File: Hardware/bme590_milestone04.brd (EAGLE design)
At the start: 100 x 80 mm, 9 parts, among them IC1 LM317LZ, U1 ARDUINOR3-DIMENSION

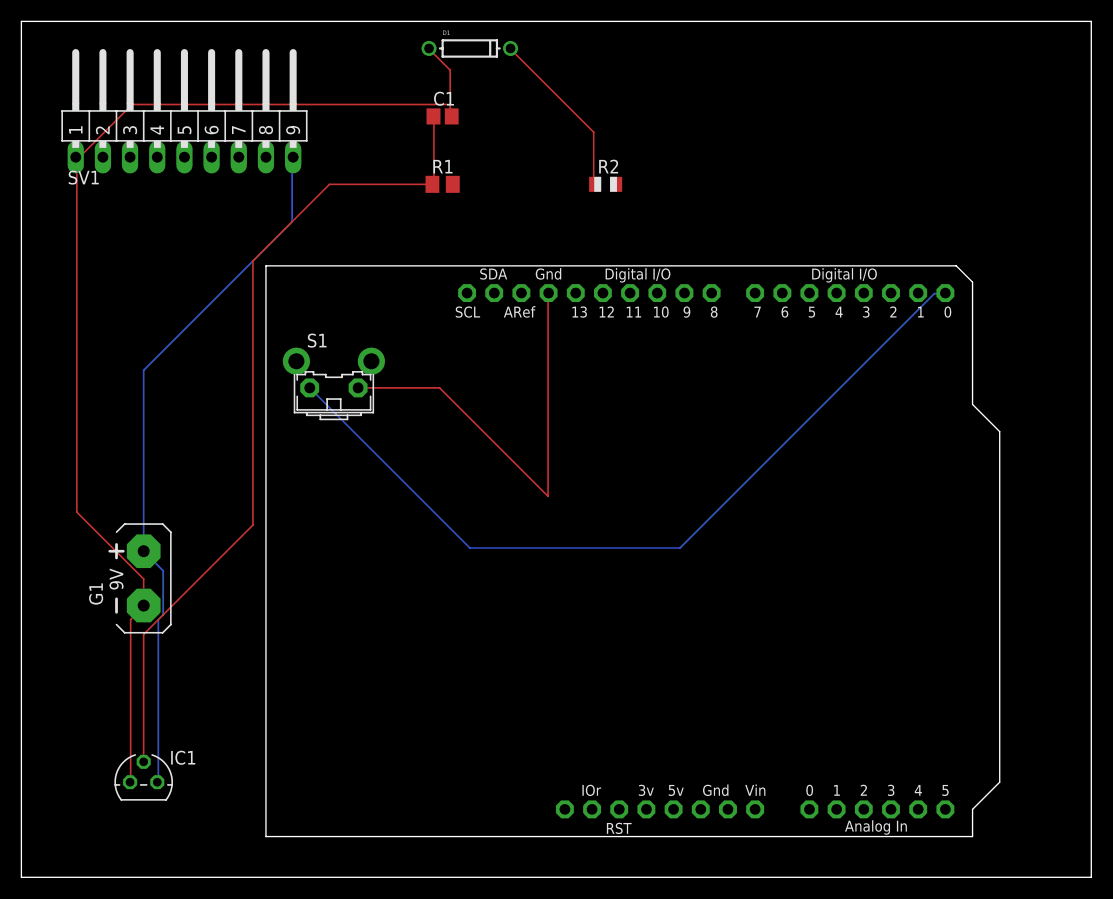
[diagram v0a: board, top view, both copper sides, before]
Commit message: updated PCB with polygon and other stuff
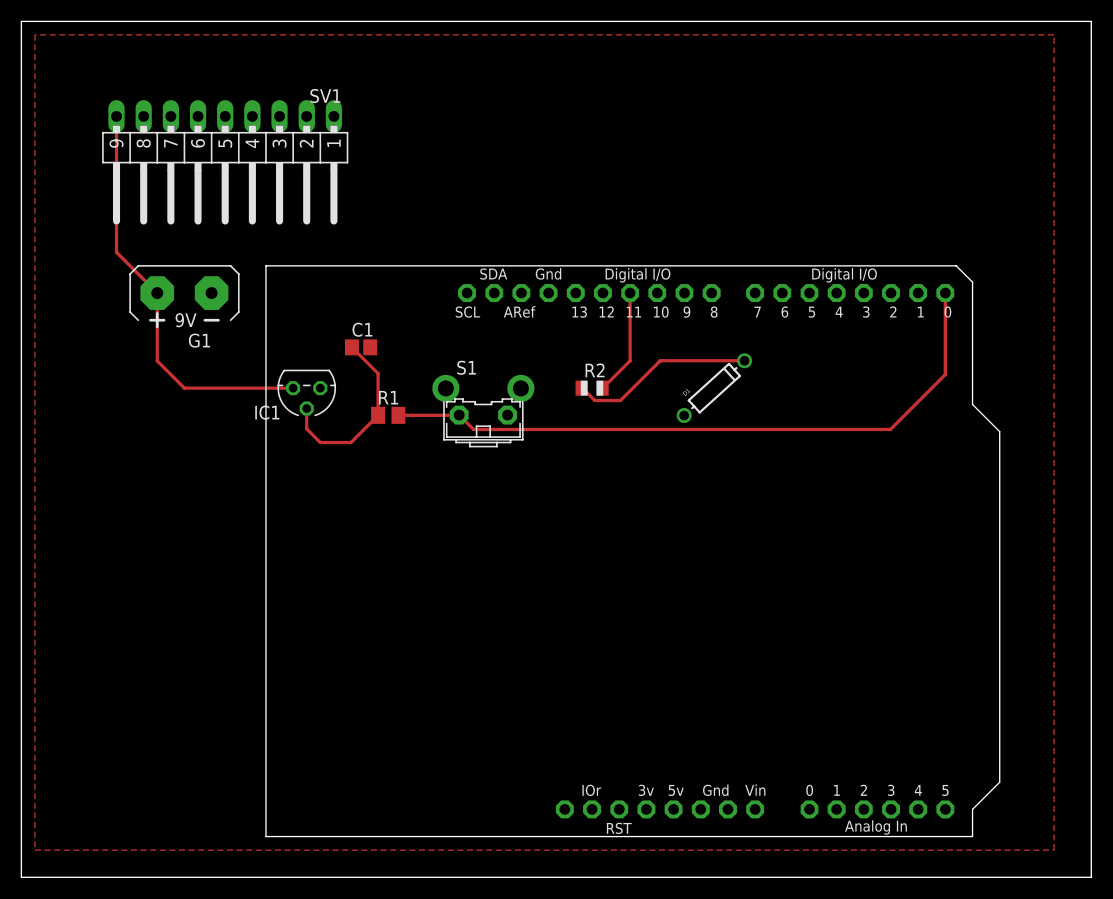
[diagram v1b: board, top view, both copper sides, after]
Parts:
- moved IC1 39.9 mm to (26.7, 45.7), turned to 180 degrees
- moved D1 39.1 mm to (64.8, 45.7), turned to 42.2 degrees
- moved G1 26.9 mm to (15.2, 54.6), turned to 90 degrees
- moved C1 22.9 mm to (31.8, 49.5)
- moved R1 22.2 mm to (34.3, 43.2)
- moved R2 19.1 mm to (53.3, 45.7)
- moved S1 14.2 mm to (43.2, 44.5)
- moved SV1 5.39 mm to (19.1, 71.1), turned to 180 degrees
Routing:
- net GND: track 146.8 -> 0.04 mm
- net N$3: track 77.3 -> 17.5 mm
- net N$1: track 65.2 -> 38.2 mm
- net N$4: track 75.5 -> 61.4 mm
- net N$2: track 0.00 -> 10.2 mm
- net N$5: track 16.0 -> 17.3 mm
- added copper zone on layer 1, net GND
